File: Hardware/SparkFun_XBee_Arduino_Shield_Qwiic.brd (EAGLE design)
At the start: 53.3 x 59.7 mm, 184 parts, among them J4 QWIIC_RIGHT_ANGLE, Q1 20V/4.2A/52mΩ/1.4W, Q2 20V/4.2A/52mΩ/1.4W, Q3 3.1A/30V/105mΩ, Q4 5.8A/30V/35mΩ, Q5 20V/4.2A/52mΩ/1.4W, U1 FSUSB30MUX_MSOP10, U2 AP63203, U3 ESD Diode, U4 FT231XS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

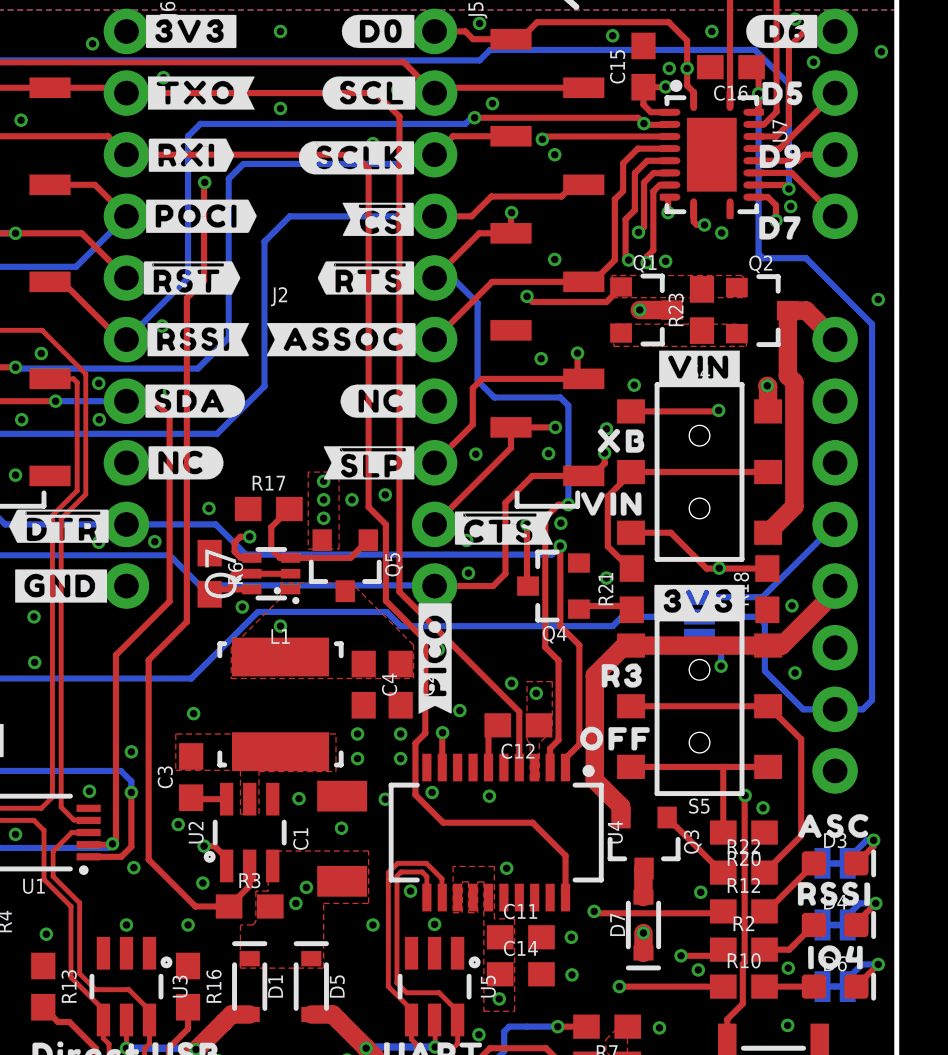
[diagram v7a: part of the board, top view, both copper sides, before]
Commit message: Adds new switch
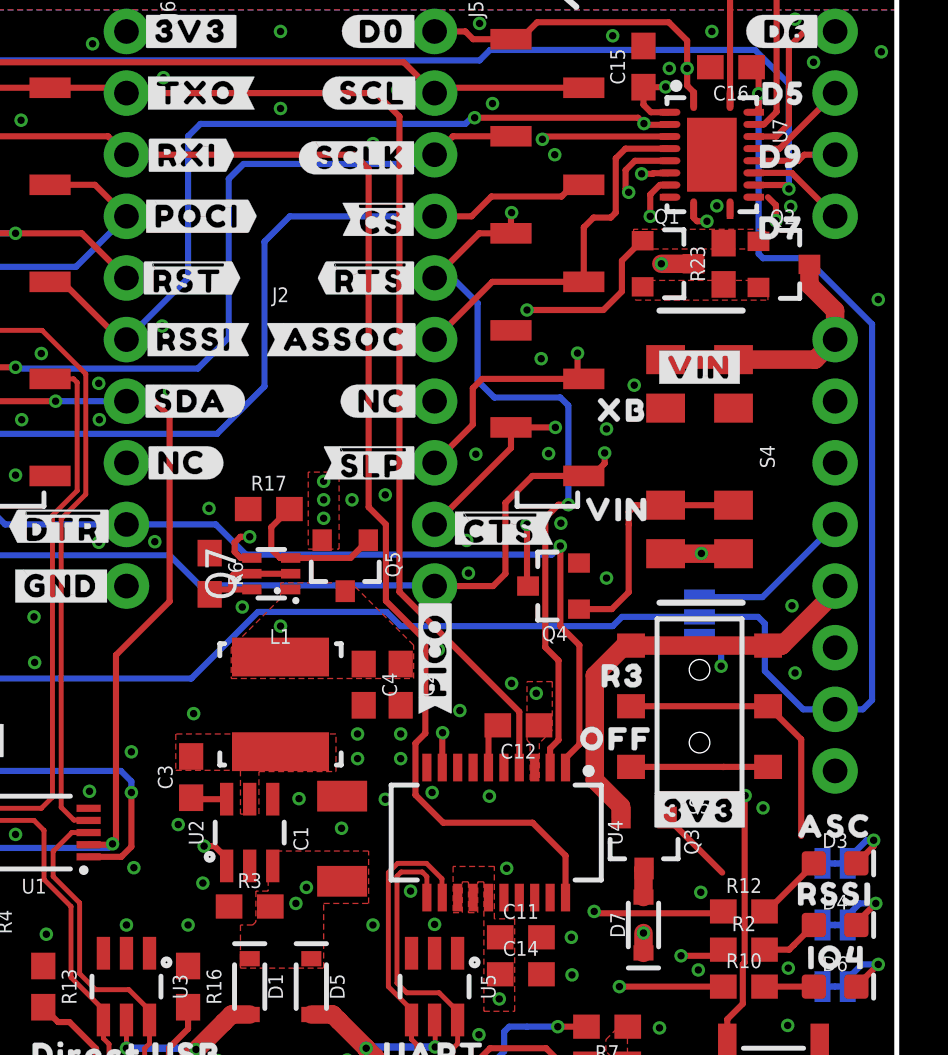
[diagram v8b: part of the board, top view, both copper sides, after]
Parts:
- removed R18, R20, R21, R22: 10k, SparkFun-Resistors:0603
- S4: value (none) -> SWITCH_DP3T; device SparkFun-Switches:SWITCH_DPDT_SMD_AYZ0202 -> DP3T:SWITCH_DP3T_SMD_JWING
- moved U$44 8.64 mm to (45.2, 17.4)
- moved Q1 2.10 mm to (43.9, 40.0)
- moved U$42 2.10 mm to (45.5, 40.2)
- moved Q2 2.10 mm to (48.6, 39.9)
- moved R23 2.10 mm to (46.2, 40.0)
- moved U$87 1.27 mm to (42.0, 33.9)
- moved S4 0.63 mm to (45.2, 32.0)
- moved U$70 0.31 mm to (41.8, 29.8)
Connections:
- net N$18 renamed GATE
- removed net N$26: R22.2, S5.2, S5.5
- removed net N$9: R21.2, S4.2, S4.5
- removed net OFF_3V3: R20.2, S5.1, S5.4
- removed net OFF_XB: R18.2, S4.4, S4.6
- net EN: no longer U7.9
- net EN_TRANS: no longer U7.12
- net GND: now also S4.P2, S4.P6, S5.1, S5.4; no longer R18.1, R20.1
- net N$22: now also S4.P3, S4.P7; no longer R21.1
- net N$27: now also S5.2, S5.5; no longer R22.1
- net VIN: now also S4.P4, S4.P8; no longer S4.1
- net VIN_R3: now also S4.P1, S4.P5; no longer S4.3
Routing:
- net EN: track 55.7 -> 0.00 mm, vias 2 -> 0
- net OFF_XB: track 16.4 -> 0.00 mm, vias 2 -> 0
- net N$26: track 13.7 -> 0.00 mm
- net N$27: track 3.26 -> 14.8 mm
- net N$9: track 10.5 -> 0.00 mm
- net OFF_3V3: track 8.36 -> 0.00 mm
- net N$22: track 2.29 -> 10.3 mm
- net GND: track 4.58 -> 10.2 mm, vias 128 -> 126
- net VIN: track 39.7 -> 41.7 mm
- net GATE: track 16.2 -> 18.1 mm
- net D7/!CTS!: track 33.5 -> 34.8 mm
- net VIN_R3: track 12.2 -> 10.9 mm
- net D9/!SLEEP!: track 19.8 -> 20.8 mm
- net D8/!DTR!: track 54.7 -> 55.6 mm
